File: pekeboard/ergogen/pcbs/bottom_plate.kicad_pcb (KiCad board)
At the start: 2 copper layers, 161.8 x 135.1 mm, 0 parts

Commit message: pekeboard cases
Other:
- outline, holes or cut-outs redrawn
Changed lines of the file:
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@@
   (title_block
     (title "bottom_plate")
-    (date "2026-03-16")
+    (date "2026-04-04")
     (rev "0.0.0")
     (company "pedroren")
@@
 (gr_line (start 249.22744472247615 137.73894786929668) (end 217.090504550722 120.67288596545656) (layer Edge.Cuts) (stroke (width 0.15) (type default)))
 (gr_line (start 216.06847480534455 119.30423362397005) (end 213.8399464960453 108.32185967448117) (layer Edge.Cuts) (stroke (width 0.15) (type default)))
-(gr_line (start 213.8 107.92412829397051) (end 213.8 101.5754694) (layer Edge.Cuts) (stroke (width 0.15) (type default)))
+(gr_line (start 213.8 107.92412829397051) (end 213.8 92.51635530000001) (layer Edge.Cuts) (stroke (width 0.15) (type default)))
+(gr_line (start 213.8 41.7836447) (end 213.8 39.216248890562504) (layer Edge.Cuts) (stroke (width 0.15) (type default)))
 (gr_line (start 212.24945219494984 37.2674049124603) (end 174.02181472909618 28.451156021897802) (layer Edge.Cuts) (stroke (width 0.15) (type default)))
 (gr_line (start 173.57236253414635 28.4) (end 148.8330047759124 28.4) (layer Edge.Cuts) (stroke (width 0.15) (type default)))
@@
 (gr_arc (start 216.06847480929926 119.30423364345934) (mid 216.42602550929925 120.10315794345934) (end 217.09050460929924 120.67288594345935) (layer Edge.Cuts) (stroke (width 0.15) (type default)))
 (gr_arc (start 213.8 107.92412829397051) (mid 213.81001170000002 108.12399449397051) (end 213.83994650000002 108.32185969397051) (layer Edge.Cuts) (stroke (width 0.15) (type default)))
-(gr_arc (start 213.0262767 37.6362977905625) (mid 212.65792620000002 37.409604890562505) (end 212.2494522 37.2674048905625) (layer Edge.Cuts) (stroke (width 0.15) (type default)))
+(gr_arc (start 213.8 39.216248890562504) (mid 213.36507260000002 37.971038990562505) (end 212.2494522 37.267404990562504) (layer Edge.Cuts) (stroke (width 0.15) (type default)))
 (gr_arc (start 174.02181473414635 28.4511561) (mid 173.79853963414635 28.4128302) (end 173.57236253414635 28.4) (layer Edge.Cuts) (stroke (width 0.15) (type default)))
 (gr_arc (start 148.8330047759124 28.4) (mid 148.5045220759124 28.4271596) (end 148.1849607759124 28.5079009) (layer Edge.Cuts) (stroke (width 0.15) (type default)))
@@
 (gr_arc (start 124.15208608395062 47.39999999999998) (mid 125.40048218395061 46.96253229999998) (end 126.10274528395063 45.841507199999974) (layer Edge.Cuts) (stroke (width 0.15) (type default)))
 (gr_arc (start 90.5 47.4) (mid 89.0857864 47.985786399999995) (end 88.5 49.4) (layer Edge.Cuts) (stroke (width 0.15) (type default)))
-(gr_line (start 215.1355 101.805) (end 236.94850000000002 101.805) (layer Edge.Cuts) (stroke (width 0.15) (type default)))
-(gr_arc (start 236.94850000000002 101.805) (mid 239.77692710000002 100.6334271) (end 240.94850000000002 97.805) (layer Edge.Cuts) (stroke (width 0.15) (type default)))
-(gr_line (start 240.94850000000002 97.805) (end 240.94850000000002 41.035000000000004) (layer Edge.Cuts) (stroke (width 0.15) (type default)))
-(gr_arc (start 240.94850000000002 41.035000000000004) (mid 239.77692710000002 38.206572900000005) (end 236.94850000000002 37.035000000000004) (layer Edge.Cuts) (stroke (width 0.15) (type default)))
-(gr_line (start 236.94850000000002 37.03500000000001) (end 215.1355 37.03500000000001) (layer Edge.Cuts) (stroke (width 0.15) (type default)))
-(gr_arc (start 215.1355 37.03500000000001) (mid 214.0388708 37.18826050000001) (end 213.0262767 37.63629780000001) (layer Edge.Cuts) (stroke (width 0.15) (type default)))
-(gr_arc (start 213.8 101.5754694) (mid 214.45795950000002 101.74719970000001) (end 215.1355 101.805) (layer Edge.Cuts) (stroke (width 0.15) (type default)))
+(gr_line (start 215.07500000000002 92.72500000000001) (end 236.52500000000003 92.72500000000001) (layer Edge.Cuts) (stroke (width 0.15) (type default)))
+(gr_arc (start 236.52500000000003 92.72500000000001) (mid 239.35342710000003 91.55342710000001) (end 240.52500000000003 88.72500000000001) (layer Edge.Cuts) (stroke (width 0.15) (type default)))
+(gr_line (start 240.52500000000003 88.72500000000001) (end 240.52500000000003 45.57500000000001) (layer Edge.Cuts) (stroke (width 0.15) (type default)))
+(gr_arc (start 240.52500000000003 45.57500000000001) (mid 239.35342710000003 42.74657290000001) (end 236.52500000000003 41.57500000000001) (layer Edge.Cuts) (stroke (width 0.15) (type default)))
+(gr_line (start 236.52500000000003 41.575) (end 215.07500000000002 41.575) (layer Edge.Cuts) (stroke (width 0.15) (type default)))
+(gr_arc (start 215.07500000000002 41.575) (mid 214.42902060000003 41.6275058) (end 213.8 41.7836447) (layer Edge.Cuts) (stroke (width 0.15) (type default)))
+(gr_arc (start 213.8 92.51635530000001) (mid 214.42902060000003 92.6724942) (end 215.07500000000002 92.72500000000001) (layer Edge.Cuts) (stroke (width 0.15) (type default)))
 (gr_circle (center 130.5 56.25) (end 132 56.25) (layer Edge.Cuts) (stroke (width 0.15) (type default)) (fill none))
 (gr_circle (center 131.4 118.1) (end 132.9 118.1) (layer Edge.Cuts) (stroke (width 0.15) (type default)) (fill none))

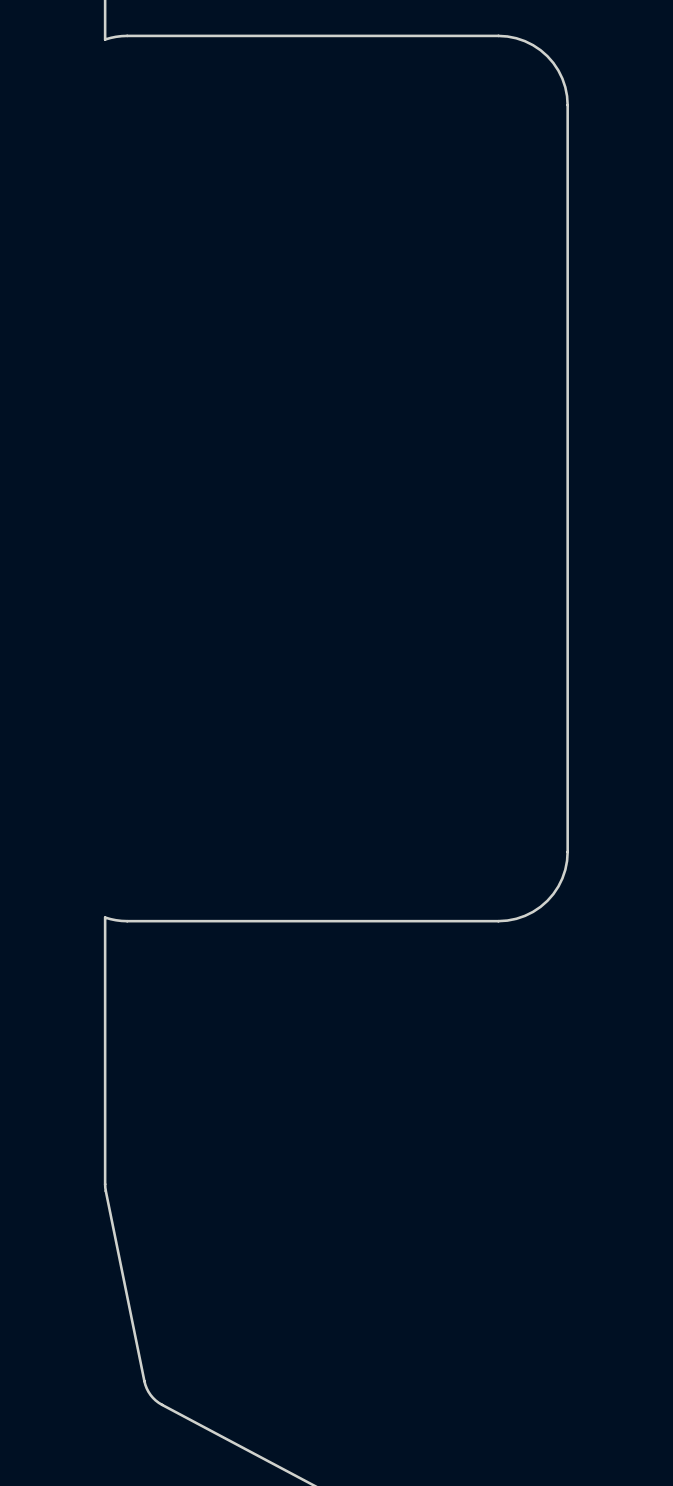
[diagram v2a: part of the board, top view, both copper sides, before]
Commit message: Battery area and cover
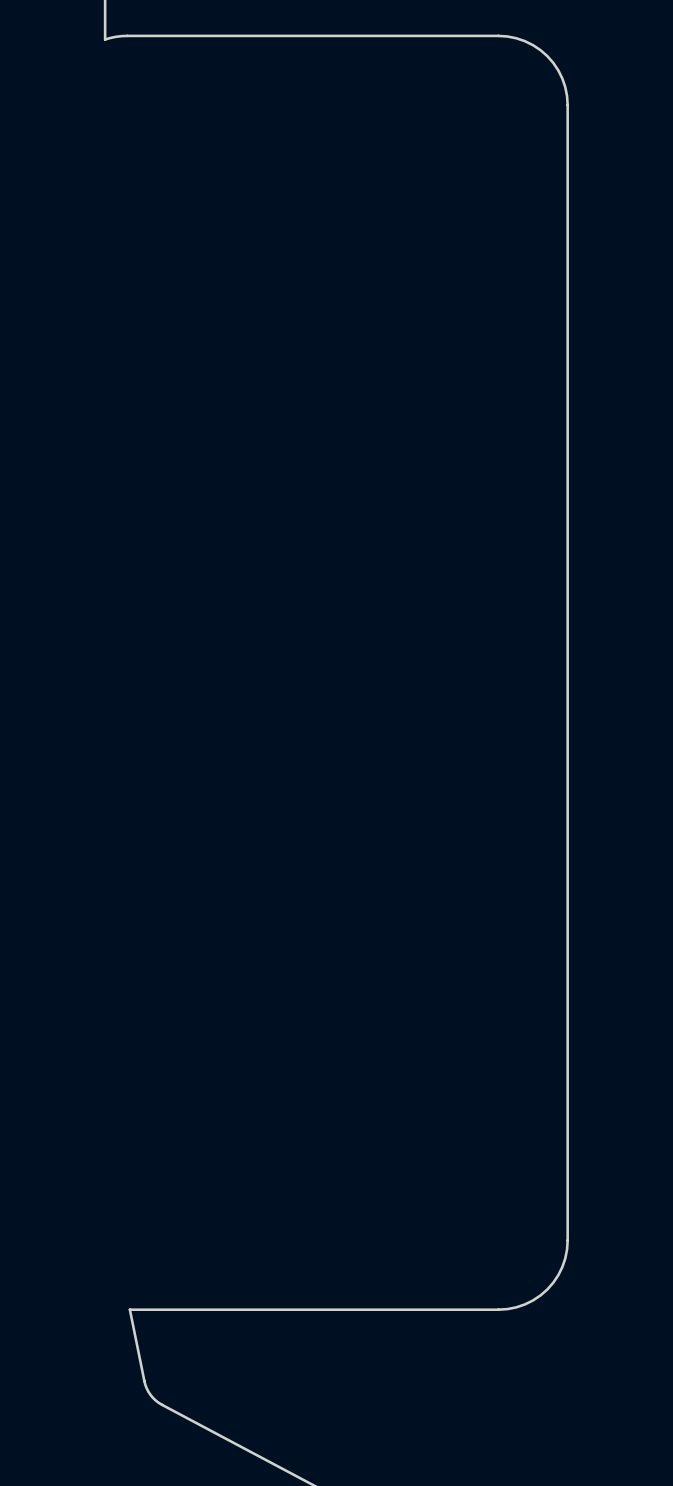
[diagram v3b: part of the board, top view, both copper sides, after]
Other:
- outline, holes or cut-outs redrawn
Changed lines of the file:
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@@
 (gr_line (start 237.3302355022819 162.4871975457507) (end 250.02147176389892 140.5053315912939) (layer Edge.Cuts) (stroke (width 0.15) (type default)))
 (gr_line (start 249.22744472247615 137.73894786929668) (end 217.090504550722 120.67288596545656) (layer Edge.Cuts) (stroke (width 0.15) (type default)))
-(gr_line (start 216.06847480534455 119.30423362397005) (end 213.8399464960453 108.32185967448117) (layer Edge.Cuts) (stroke (width 0.15) (type default)))
-(gr_line (start 213.8 107.92412829397051) (end 213.8 92.51635530000001) (layer Edge.Cuts) (stroke (width 0.15) (type default)))
+(gr_line (start 216.06847480534455 119.30423362397005) (end 215.23057636289022 115.17499999999995) (layer Edge.Cuts) (stroke (width 0.15) (type default)))
 (gr_line (start 213.8 41.7836447) (end 213.8 39.216248890562504) (layer Edge.Cuts) (stroke (width 0.15) (type default)))
 (gr_line (start 212.24945219494984 37.2674049124603) (end 174.02181472909618 28.451156021897802) (layer Edge.Cuts) (stroke (width 0.15) (type default)))
@@
 (gr_arc (start 250.02147176389894 140.5053315912939) (mid 250.21180076389894 138.9535564912939) (end 249.22744476389894 137.7389478912939) (layer Edge.Cuts) (stroke (width 0.15) (type default)))
 (gr_arc (start 216.06847480929926 119.30423364345934) (mid 216.42602550929925 120.10315794345934) (end 217.09050460929924 120.67288594345935) (layer Edge.Cuts) (stroke (width 0.15) (type default)))
-(gr_arc (start 213.8 107.92412829397051) (mid 213.81001170000002 108.12399449397051) (end 213.83994650000002 108.32185969397051) (layer Edge.Cuts) (stroke (width 0.15) (type default)))
 (gr_arc (start 213.8 39.216248890562504) (mid 213.36507260000002 37.971038990562505) (end 212.2494522 37.267404990562504) (layer Edge.Cuts) (stroke (width 0.15) (type default)))
 (gr_arc (start 174.02181473414635 28.4511561) (mid 173.79853963414635 28.4128302) (end 173.57236253414635 28.4) (layer Edge.Cuts) (stroke (width 0.15) (type default)))
@@
 (gr_arc (start 124.15208608395062 47.39999999999998) (mid 125.40048218395061 46.96253229999998) (end 126.10274528395063 45.841507199999974) (layer Edge.Cuts) (stroke (width 0.15) (type default)))
 (gr_arc (start 90.5 47.4) (mid 89.0857864 47.985786399999995) (end 88.5 49.4) (layer Edge.Cuts) (stroke (width 0.15) (type default)))
-(gr_line (start 215.07500000000002 92.72500000000001) (end 236.52500000000003 92.72500000000001) (layer Edge.Cuts) (stroke (width 0.15) (type default)))
-(gr_arc (start 236.52500000000003 92.72500000000001) (mid 239.35342710000003 91.55342710000001) (end 240.52500000000003 88.72500000000001) (layer Edge.Cuts) (stroke (width 0.15) (type default)))
-(gr_line (start 240.52500000000003 88.72500000000001) (end 240.52500000000003 45.57500000000001) (layer Edge.Cuts) (stroke (width 0.15) (type default)))
+(gr_line (start 240.52500000000003 111.175) (end 240.52500000000003 45.57500000000001) (layer Edge.Cuts) (stroke (width 0.15) (type default)))
 (gr_arc (start 240.52500000000003 45.57500000000001) (mid 239.35342710000003 42.74657290000001) (end 236.52500000000003 41.57500000000001) (layer Edge.Cuts) (stroke (width 0.15) (type default)))
 (gr_line (start 236.52500000000003 41.575) (end 215.07500000000002 41.575) (layer Edge.Cuts) (stroke (width 0.15) (type default)))
 (gr_arc (start 215.07500000000002 41.575) (mid 214.42902060000003 41.6275058) (end 213.8 41.7836447) (layer Edge.Cuts) (stroke (width 0.15) (type default)))
-(gr_arc (start 213.8 92.51635530000001) (mid 214.42902060000003 92.6724942) (end 215.07500000000002 92.72500000000001) (layer Edge.Cuts) (stroke (width 0.15) (type default)))
 (gr_circle (center 130.5 56.25) (end 132 56.25) (layer Edge.Cuts) (stroke (width 0.15) (type default)) (fill none))
 (gr_circle (center 131.4 118.1) (end 132.9 118.1) (layer Edge.Cuts) (stroke (width 0.15) (type default)) (fill none))
@@
 (gr_circle (center 175.25 119.05) (end 176.75 119.05) (layer Edge.Cuts) (stroke (width 0.15) (type default)) (fill none))
 (gr_circle (center 221.88370139999998 138.84137940000002) (end 223.38370139999998 138.84137940000002) (layer Edge.Cuts) (stroke (width 0.15) (type default)) (fill none))
+(gr_line (start 215.23057636289022 115.175) (end 236.52500000000003 115.175) (layer Edge.Cuts) (stroke (width 0.15) (type default)))
+(gr_arc (start 236.52500000000003 115.175) (mid 239.35342710000003 114.0034271) (end 240.52500000000003 111.175) (layer Edge.Cuts) (stroke (width 0.15) (type default)))
 )

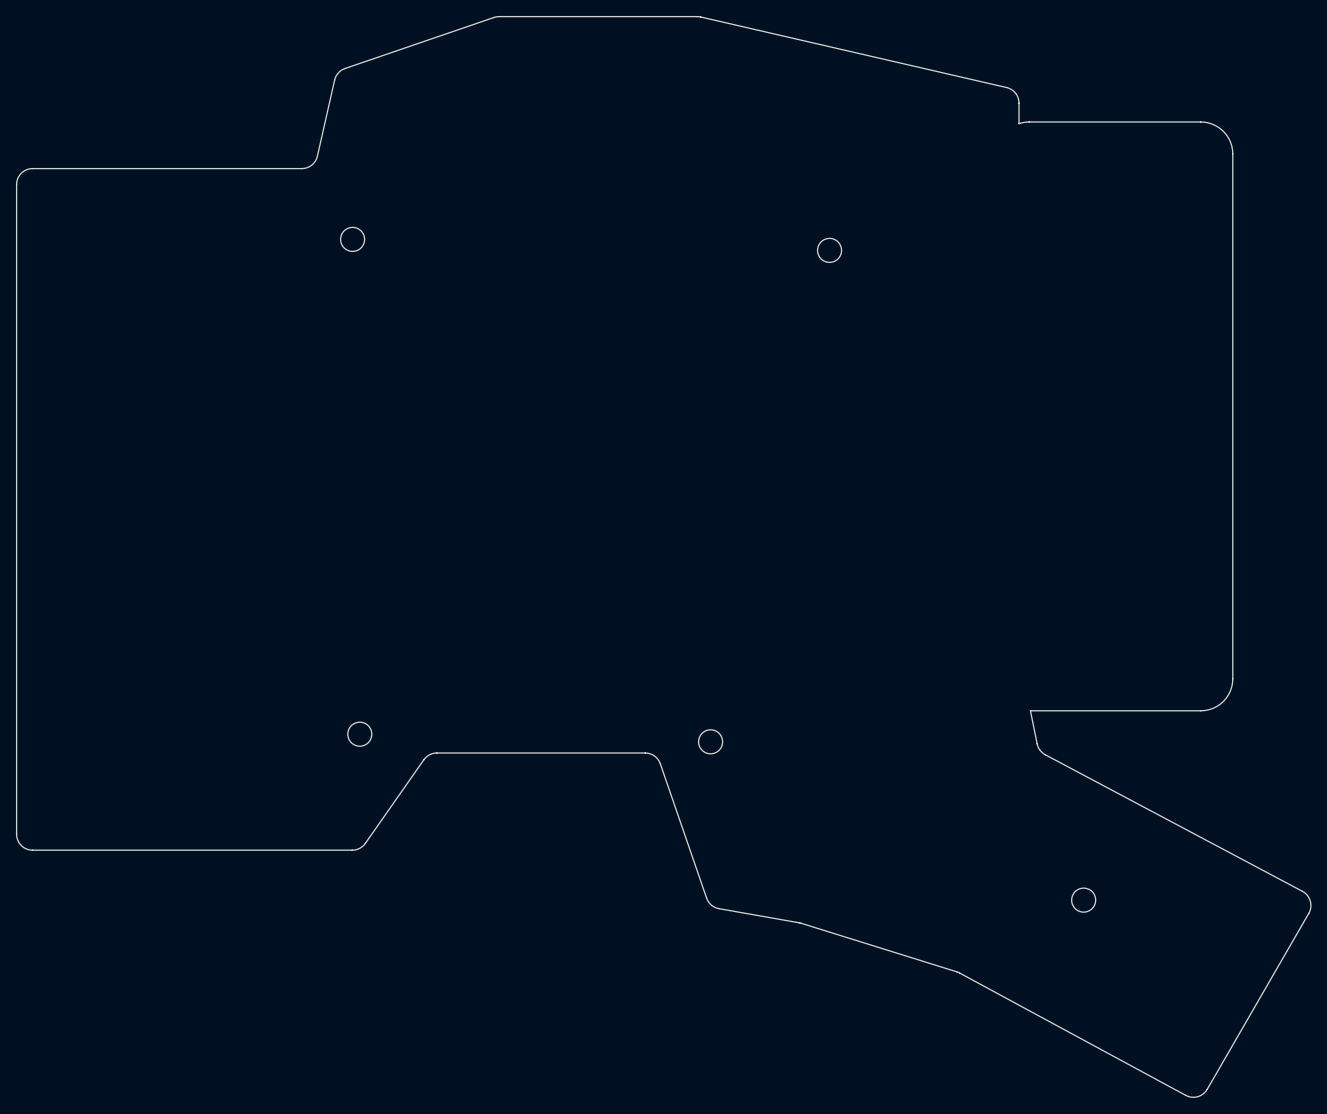
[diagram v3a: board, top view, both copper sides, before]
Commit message: Fixing keys spacing More case and battery space refinements
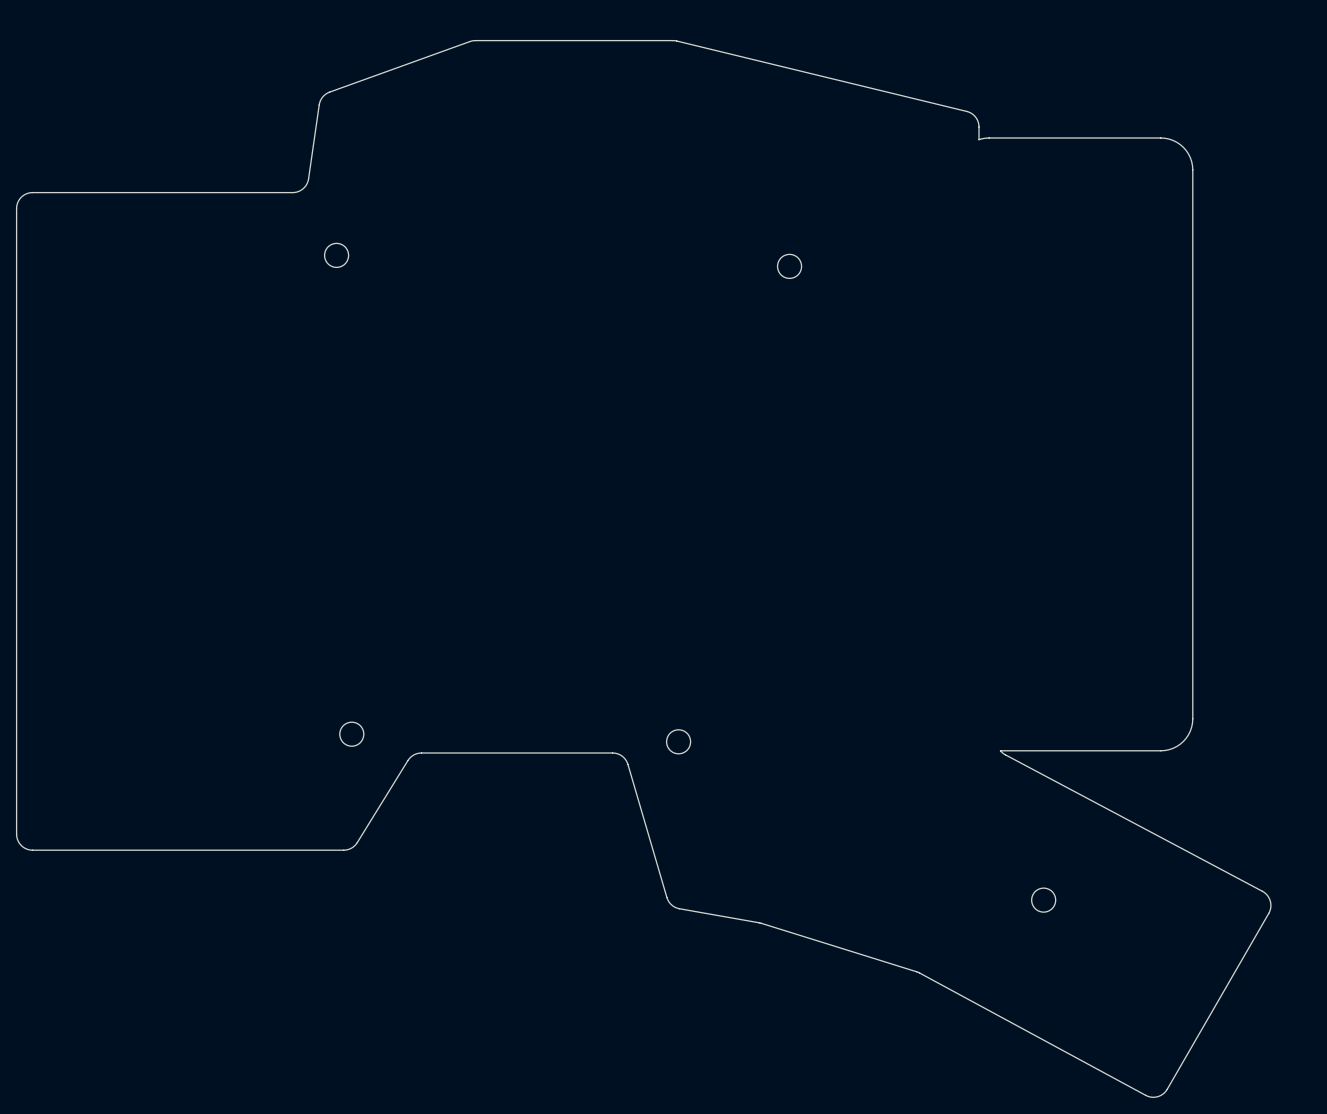
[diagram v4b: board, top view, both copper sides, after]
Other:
- board size 161.8 x 135.1 mm -> 156.8 x 132.1 mm

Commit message: Extreme trimming
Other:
- board size 156.8 x 132.1 mm -> 150.9 x 124.7 mm
